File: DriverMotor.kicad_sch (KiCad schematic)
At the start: 20 parts, among them U3 DRV8874PWPR

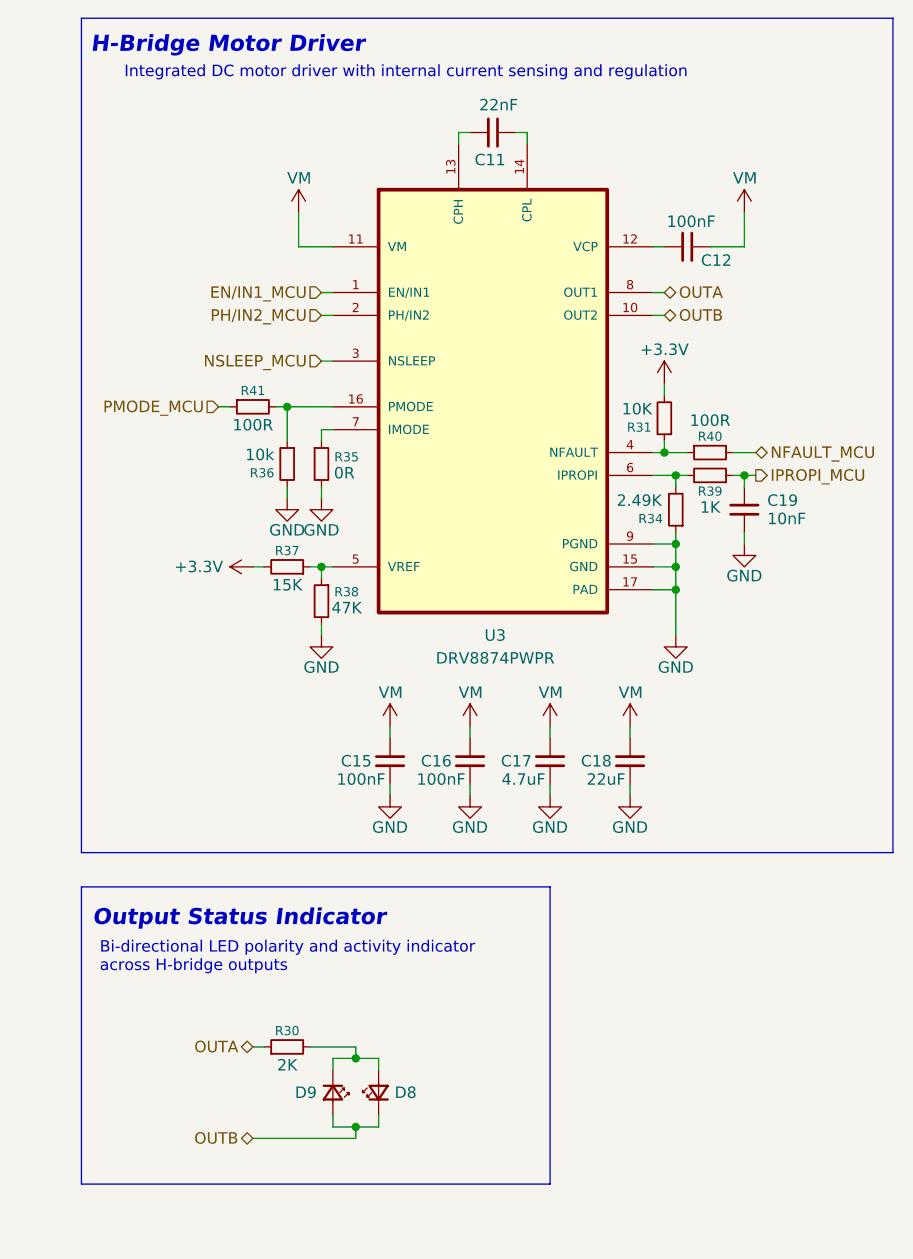
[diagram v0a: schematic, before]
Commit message: feat(hw): add asymmetrical RC pulse stretcher for UART TX/RX activity LEDs
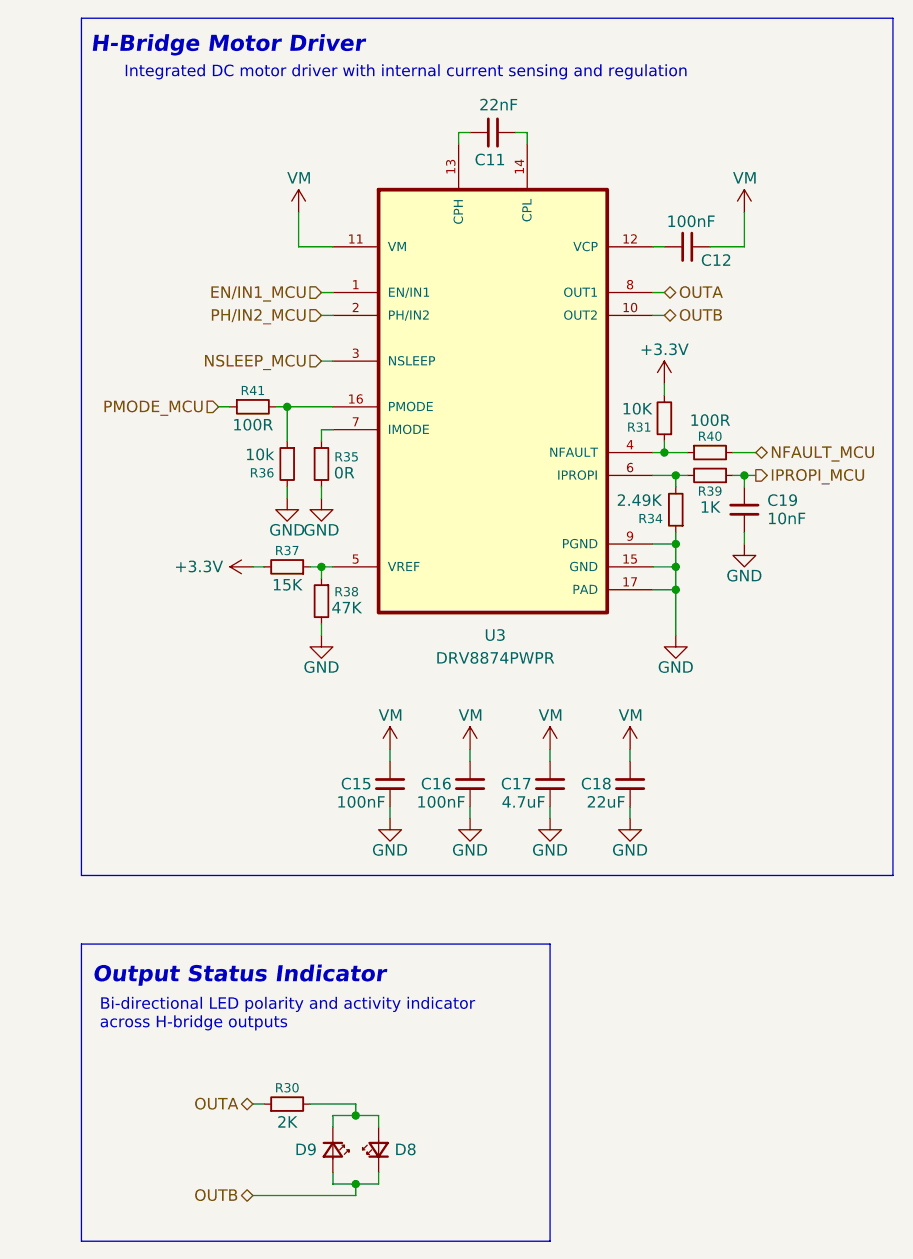
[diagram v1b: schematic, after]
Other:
- moved on the sheet: C15, C16, C17, C18, D8, D9, R30

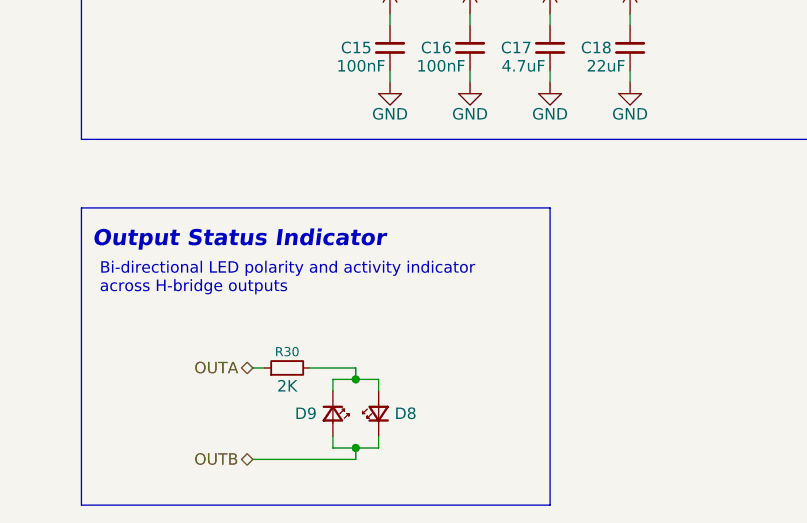
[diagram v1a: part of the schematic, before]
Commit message: feat:add power sheat
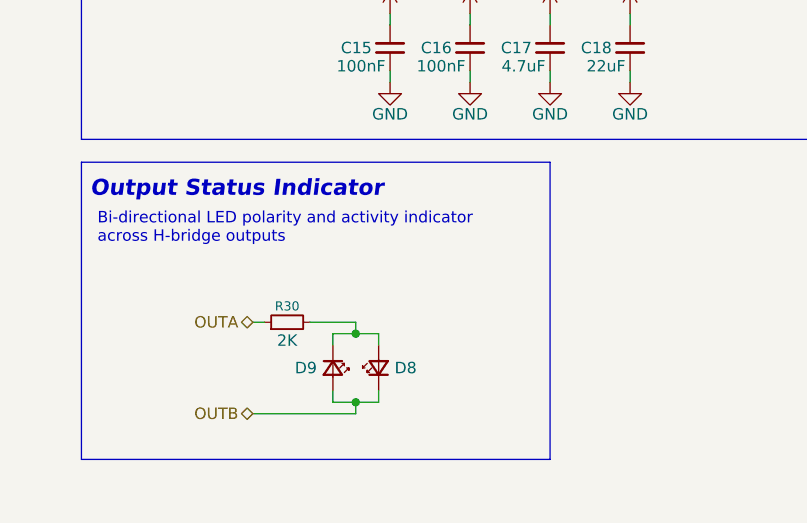
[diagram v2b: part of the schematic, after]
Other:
- moved on the sheet: D8, D9, R30
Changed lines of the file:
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@@
 	)
 	(rectangle
-		(start 36.83 149.86)
-		(end 88.9 182.88)
+		(start 36.83 144.78)
+		(end 88.9 177.8)
 		(stroke
 			(width 0.0508)
@@
 	(text "Output Status Indicator"
 		(exclude_from_sim no)
-		(at 54.356 153.416 0)
+		(at 54.102 147.828 0)
 		(effects
 			(font
@@
 	(text "Bi-directional LED polarity and activity indicator\nacross H-bridge outputs"
 		(exclude_from_sim no)
-		(at 38.862 157.734 0)
+		(at 38.608 152.146 0)
 		(effects
 			(font
@@
 	)
 	(junction
-		(at 67.31 176.53)
+		(at 67.31 171.45)
 		(diameter 0)
 		(color 0 0 0 0)
 	)
 	(junction
-		(at 67.31 168.91)
+		(at 67.31 163.83)
 		(diameter 0)
 		(color 0 0 0 0)
@@
 	(wire
 		(pts
-			(xy 64.77 175.26) (xy 64.77 176.53)
+			(xy 64.77 170.18) (xy 64.77 171.45)
 		)
 		(stroke
@@
 	(wire
 		(pts
-			(xy 62.23 167.64) (xy 67.31 167.64)
+			(xy 62.23 162.56) (xy 67.31 162.56)
 		)
 		(stroke
@@
 	(wire
 		(pts
-			(xy 67.31 177.8) (xy 67.31 176.53)
+			(xy 67.31 172.72) (xy 67.31 171.45)
 		)
 		(stroke
@@
 	(wire
 		(pts
-			(xy 64.77 168.91) (xy 67.31 168.91)
+			(xy 64.77 163.83) (xy 67.31 163.83)
 		)
 		(stroke
@@
 	(wire
 		(pts
-			(xy 67.31 167.64) (xy 67.31 168.91)
+			(xy 67.31 162.56) (xy 67.31 163.83)
 		)
 		(stroke
@@
 	(wire
 		(pts
-			(xy 55.88 177.8) (xy 67.31 177.8)
+			(xy 55.88 172.72) (xy 67.31 172.72)
 		)
 		(stroke
@@
 	(wire
 		(pts
-			(xy 64.77 170.18) (xy 64.77 168.91)
+			(xy 64.77 165.1) (xy 64.77 163.83)
 		)
 		(stroke
@@
 	(wire
 		(pts
-			(xy 55.88 167.64) (xy 57.15 167.64)
+			(xy 55.88 162.56) (xy 57.15 162.56)
 		)
 		(stroke
@@
 	(wire
 		(pts
-			(xy 69.85 175.26) (xy 69.85 176.53)
+			(xy 69.85 170.18) (xy 69.85 171.45)
 		)
 		(stroke
@@
 	(wire
 		(pts
-			(xy 67.31 168.91) (xy 69.85 168.91)
+			(xy 67.31 163.83) (xy 69.85 163.83)
 		)
 		(stroke
@@
 	(wire
 		(pts
-			(xy 69.85 168.91) (xy 69.85 170.18)
+			(xy 69.85 163.83) (xy 69.85 165.1)
 		)
 		(stroke
@@
 	(wire
 		(pts
-			(xy 64.77 176.53) (xy 67.31 176.53)
+			(xy 64.77 171.45) (xy 67.31 171.45)
 		)
 		(stroke
@@
 	(wire
 		(pts
-			(xy 67.31 176.53) (xy 69.85 176.53)
+			(xy 67.31 171.45) (xy 69.85 171.45)
 		)
 		(stroke
@@
 	(hierarchical_label "OUTB"
 		(shape bidirectional)
-		(at 55.88 177.8 180)
+		(at 55.88 172.72 180)
 		(effects
 			(font
@@
 	(hierarchical_label "OUTA"
 		(shape bidirectional)
-		(at 55.88 167.64 180)
+		(at 55.88 162.56 180)
 		(effects
 			(font
@@
 	(symbol
 		(lib_id "Device:R_Small")
-		(at 59.69 167.64 90)
+		(at 59.69 162.56 90)
 		(unit 1)
 		(body_style 1)
@@
 		(dnp no)
 		(property "Reference" "R30"
-			(at 59.69 165.862 90)
+			(at 59.69 160.782 90)
 			(show_name no)
 			(do_not_autoplace no)
@@
 		)
 		(property "Value" "2K"
-			(at 59.69 169.672 90)
+			(at 59.69 164.592 90)
 			(show_name no)
 			(do_not_autoplace no)
@@
 		)
 		(property "Footprint" "Resistor_SMD:R_0603_1608Metric"
-			(at 59.69 167.64 0)
+			(at 59.69 162.56 0)
 			(hide yes)
 			(show_name no)
@@
 		)
 		(property "Datasheet" ""
-			(at 59.69 167.64 0)
+			(at 59.69 162.56 0)
 			(hide yes)
 			(show_name no)
@@
 		)
 		(property "Description" "Resistor, small symbol"
-			(at 59.69 167.64 0)
+			(at 59.69 162.56 0)
 			(hide yes)
 			(show_name no)
@@
 	(symbol
 		(lib_id "Device:LED_Small")
-		(at 64.77 172.72 270)
+		(at 64.77 167.64 270)
 		(unit 1)
 		(body_style 1)
@@
 		(dnp no)
 		(property "Reference" "D9"
-			(at 62.992 172.72 90)
+			(at 62.992 167.64 90)
 			(show_name no)
 			(do_not_autoplace no)
@@
 		)
 		(property "Value" "LED_Small"
-			(at 62.23 171.5136 90)
+			(at 62.23 166.4336 90)
 			(hide yes)
 			(show_name no)
@@
 		)
 		(property "Footprint" "LED_SMD:LED_0603_1608Metric"
-			(at 64.77 172.72 90)
+			(at 64.77 167.64 90)
 			(hide yes)
 			(show_name no)
@@
 		)
 		(property "Datasheet" ""
-			(at 64.77 172.72 90)
+			(at 64.77 167.64 90)
 			(hide yes)
 			(show_name no)
@@
 		)
 		(property "Description" "Light emitting diode, small symbol"
-			(at 64.77 172.72 0)
+			(at 64.77 167.64 0)
 			(hide yes)
 			(show_name no)
@@
 		)
 		(property "Sim.Pins" "1=K 2=A"
-			(at 64.77 172.72 0)
+			(at 64.77 167.64 0)
 			(hide yes)
 			(show_name no)
@@
 	(symbol
 		(lib_id "Device:LED_Small")
-		(at 69.85 172.72 90)
+		(at 69.85 167.64 90)
 		(unit 1)
 		(body_style 1)
@@
 		(dnp no)
 		(property "Reference" "D8"
-			(at 71.628 172.72 90)
+			(at 71.628 167.64 90)
 			(show_name no)
 			(do_not_autoplace no)
@@
 		)
 		(property "Value" "LED_Small"
-			(at 72.39 173.9264 90)
+			(at 72.39 168.8464 90)
 			(hide yes)
 			(show_name no)
@@
 		)
 		(property "Footprint" "LED_SMD:LED_0603_1608Metric"
-			(at 69.85 172.72 90)
+			(at 69.85 167.64 90)
 			(hide yes)
 			(show_name no)
@@
 		)
 		(property "Datasheet" ""
-			(at 69.85 172.72 90)
+			(at 69.85 167.64 90)
 			(hide yes)
 			(show_name no)
@@
 		)
 		(property "Description" "Light emitting diode, small symbol"
-			(at 69.85 172.72 0)
+			(at 69.85 167.64 0)
 			(hide yes)
 			(show_name no)
@@
 		)
 		(property "Sim.Pins" "1=K 2=A"
-			(at 69.85 172.72 0)
+			(at 69.85 167.64 0)
 			(hide yes)
 			(show_name no)

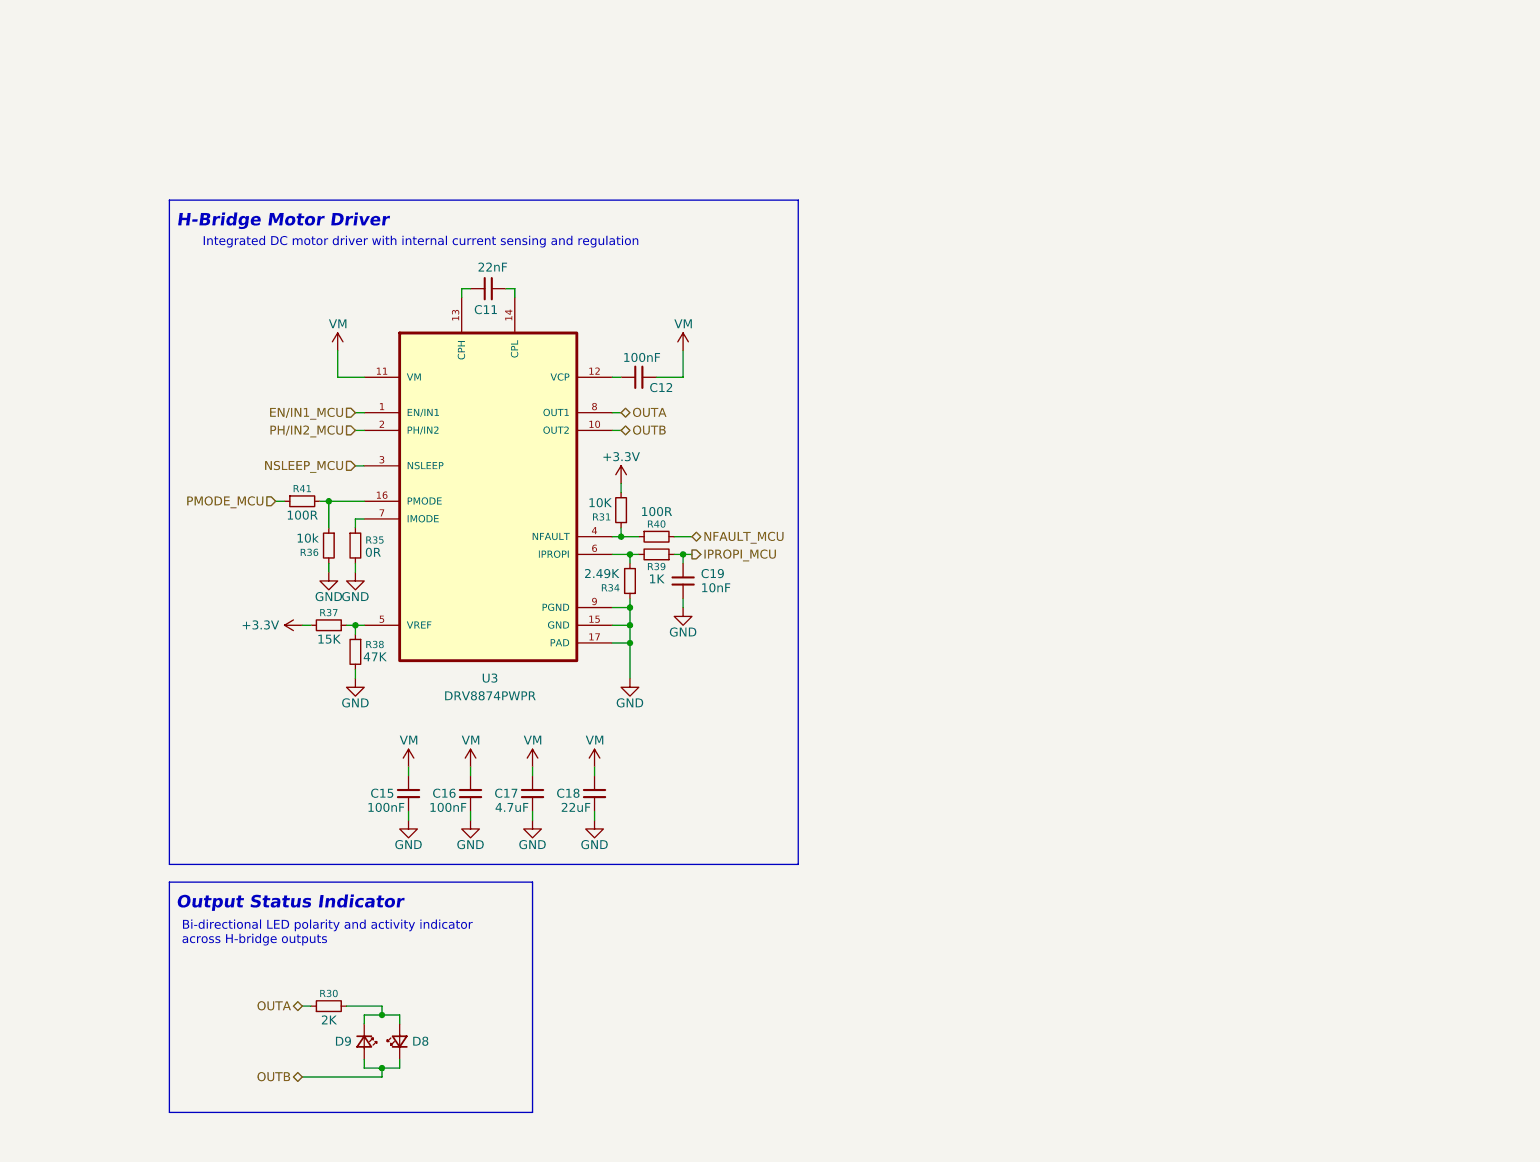
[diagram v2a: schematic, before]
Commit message: feat: add LTC4365 protection circuit and 3.3V logic LDO
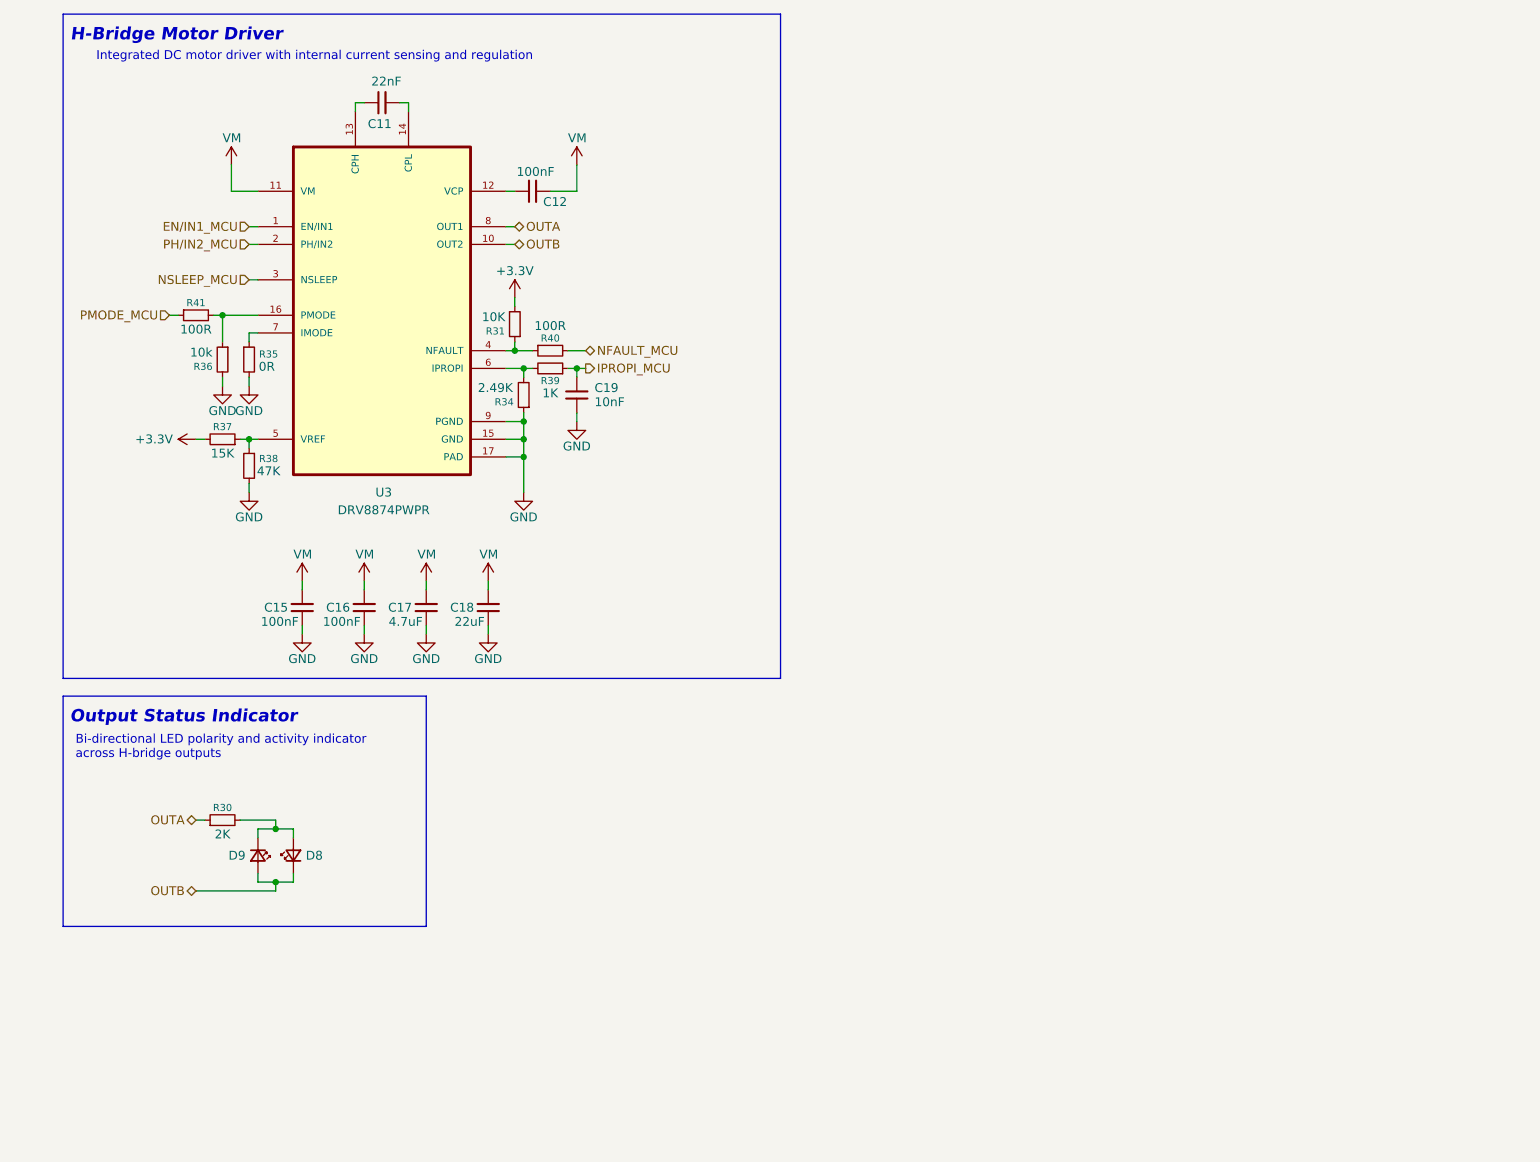
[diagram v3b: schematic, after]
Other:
- moved on the sheet: C11, C12, C15, C16, C17, C18, C19, D8, D9, R30, R31, R34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

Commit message: feat: add standardized functional notes across all schematic sheets
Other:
- title: KinetiCoreDC - DriverMotorDC -> KinetiCoreDC - Driver Motor 
- moved on the sheet: C11, C12, C15, C16, C17, C18, C19, D8, D9, R30, R31, R34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

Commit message: fix: fix some errors in shematic
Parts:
- renumbered C15 to C17, C16 to C18, C11 to C19, C17 to C20, C18 to C21, C12 to C22, C19 to C23, D9 to D10, D8 to D11, R41 to R34, R30 to R35, R35 to R38, R38 to R39, R31 to R40, R34 to R41, R40 to R42, R39 to R43, U3 to U10
